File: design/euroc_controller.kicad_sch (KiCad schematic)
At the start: 66 parts, among them J1 xt30, J2 jst_sh 4, J4 jst_sh 4, J5 jst_sh 4, J6 SMA, J8 USB_C_Receptacle_USB2.0, J9 jst_sh 4, Q1 MMBT3904, U1 TPSM5601R5, U13 STM32U575CGTx, U2 USBLC6-2SC6, U3 LSM6DSO32, U4 MS5611-01BA, U5 TCAN332, U6 W25Q128JVS, U7 RFM69W, U8 L86, Y1 48MHz

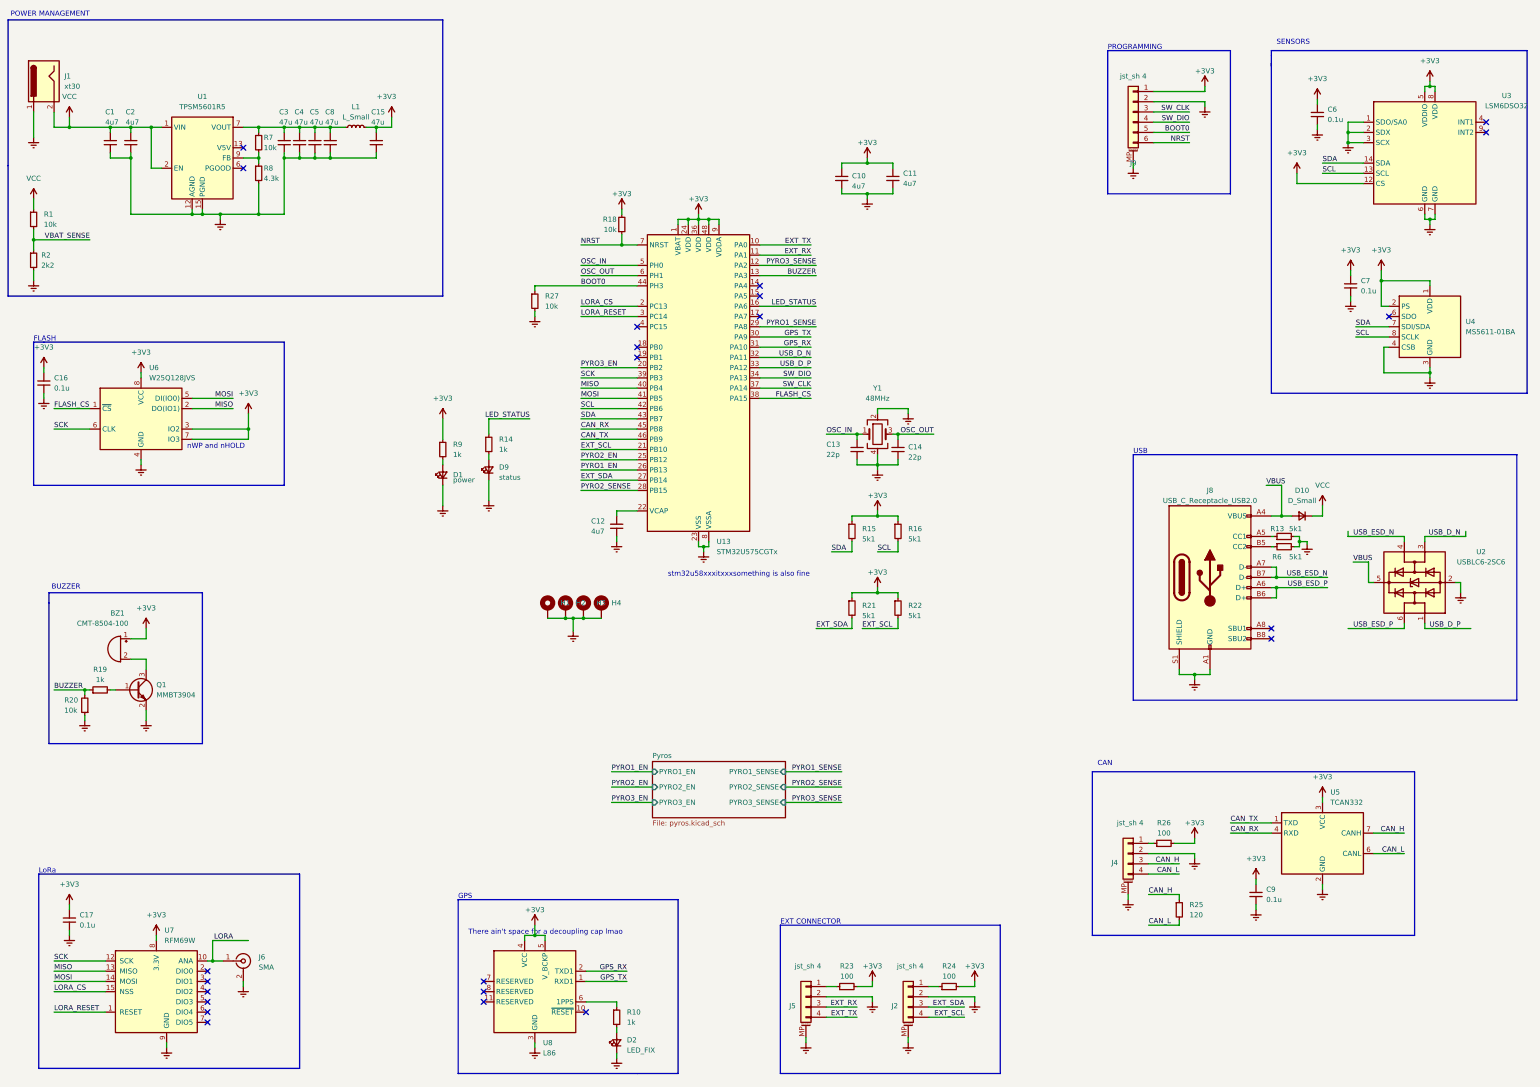
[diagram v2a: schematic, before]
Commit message: PCB 1.1 old regulator
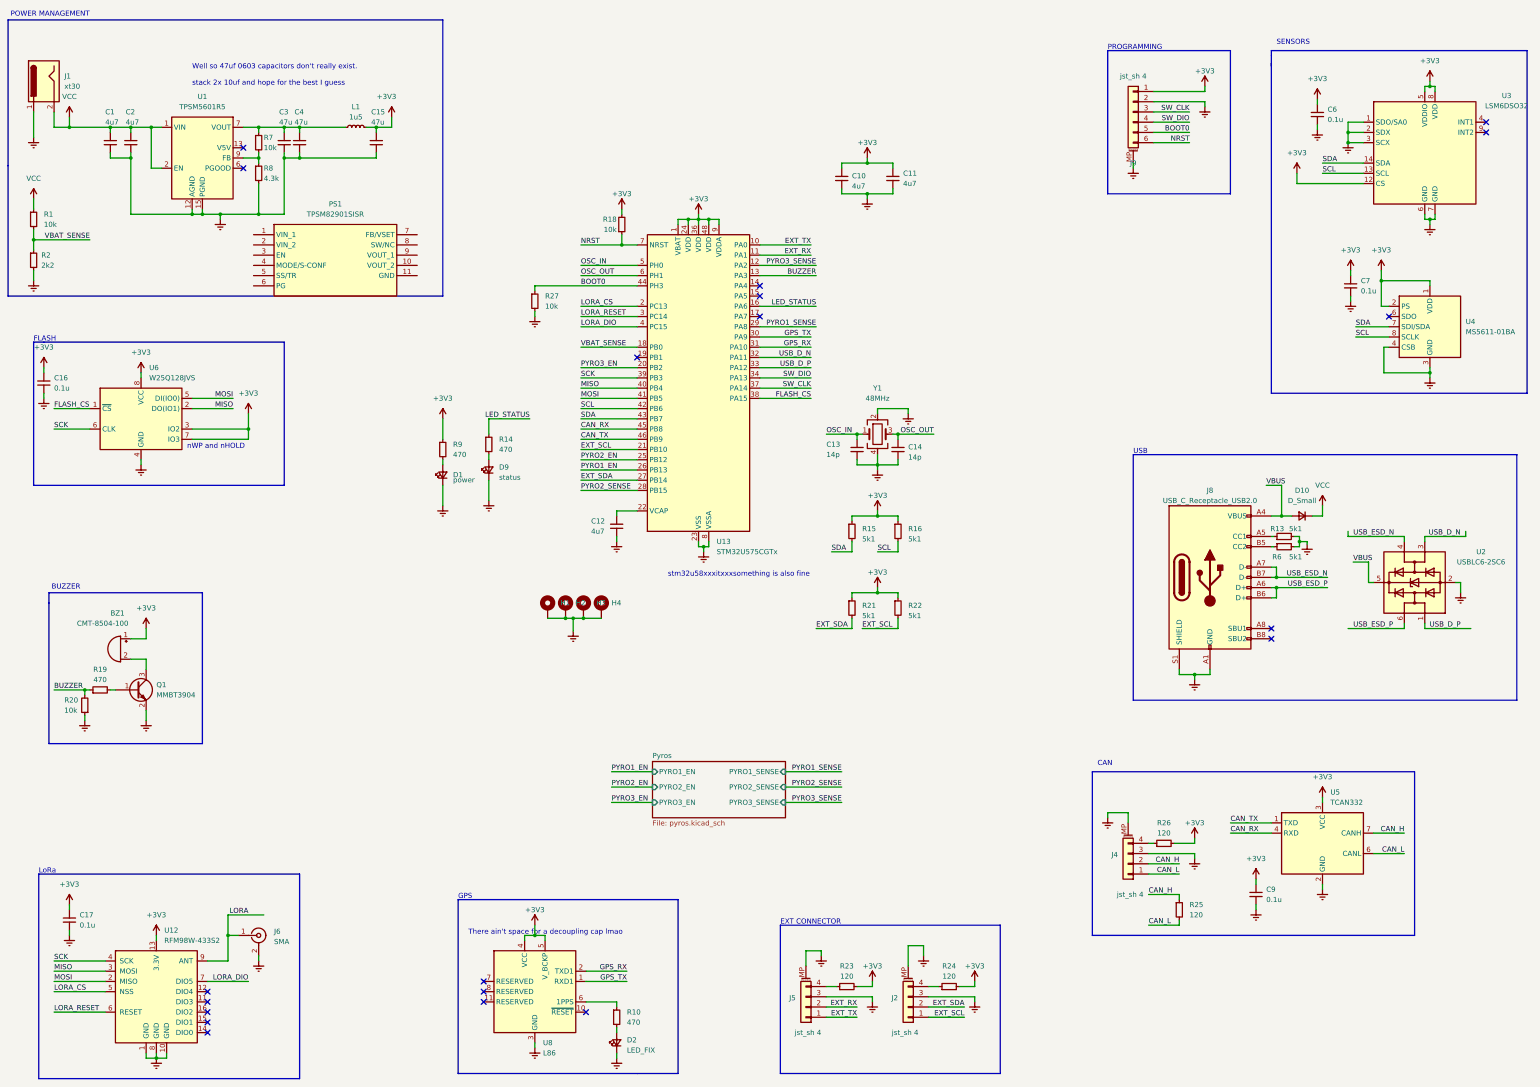
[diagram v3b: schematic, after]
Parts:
- removed C5, C8: 47u, Capacitor_SMD:C_0603_1608Metric, symbol Device:C_Small
- removed U7: RFM69W, RF_Module:HOPERF_RFM69HW, symbol RF_Module:RFM69W
- added PS1: TPSM82901SISR, lib:TPSM82901SISR, symbol TPSM82901SISR:TPSM82901SISR
- added U12: RFM98W-433S2, RF_Module:HOPERF_RFM9XW_SMD, symbol RF_Module:RFM98W-433S2
- C1, C15, C2, C3, C4: footprint Capacitor_SMD:C_0603_1608Metric -> Capacitor_SMD:C_1206_3216Metric
- C13, C14: value 22p -> 14p
- D10: mfn (none) -> BAT760-7
- J2, J4, J5: footprint Connector_JST:JST_SH_BM04B-SRSS-TB_1x04-1MP_P1.00mm_Vertical -> Connector_JST:JST_SH_SM04B-SRSS-TB_1x04-1MP_P1.00mm_Horizontal
- J8: mfn (none) -> USB4105-GF-A
- L1: value L_Small -> 1u5; footprint Inductor_SMD:L_0603_1608Metric -> Inductor_SMD:L_1206_3216Metric; mfn (none) -> MCHK1608T1R5MKN
- R10, R14, R19, R9: value 1k -> 470
- R23, R24, R26: value 100 -> 120
- Y1: mfn (none) -> CX2016SA48000H0FLJG1
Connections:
- net +3V3: now also U12.13 (3.3V)
- net CAN_H: now also J4.2 (Pin_2); no longer J4.3 (Pin_3)
- net CAN_L: now also J4.1 (Pin_1); no longer J4.4 (Pin_4)
- net EXT_RX: now also J5.2 (Pin_2); no longer J5.3 (Pin_3)
- net EXT_SCL: now also J2.1 (Pin_1); no longer J2.4 (Pin_4)
- net EXT_SDA: now also J2.2 (Pin_2); no longer J2.3 (Pin_3)
- net EXT_TX: now also J5.1 (Pin_1); no longer J5.4 (Pin_4)
- net Earth: now also J2.3 (Pin_3), J4.3 (Pin_3), J5.3 (Pin_3), U12.1 (GND), U12.10 (GND), U12.8 (GND); no longer J2.2 (Pin_2), J4.2 (Pin_2), J5.2 (Pin_2)
- net LORA: now also U12.9 (ANT)
- net LORA_CS: now also U12.5 (NSS)
- net LORA_RESET: now also U12.6 (RESET)
- net MISO: now also U12.3 (MOSI)
- net MOSI: now also U12.2 (MISO)
- net SCK: now also U12.4 (SCK)
- net VBAT_SENSE: now also U13.18 (PB0)
- net at R24.1: now also J2.4 (Pin_4); no longer J2.1 (Pin_1)
- net at R26.1: now also J4.4 (Pin_4); no longer J4.1 (Pin_1)
- net at R23.1: now also J5.4 (Pin_4); no longer J5.1 (Pin_1)
- net LORA_DIO: now reaches U13.4 (PC15)
- net LORA_DIO: now also U12.7 (DIO5)
- no-connect marks 23 -> 20
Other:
- note added: "Well so 47uf 0603 capacitors don't really exist. stack 2x 10uf and hope for the best I guess"
- moved on the sheet: J2, J4, J5, J6

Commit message: PCB v1.1
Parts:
- removed C15: 47u, Capacitor_SMD:C_1206_3216Metric, symbol Device:C_Small
- removed U1: TPSM5601R5, Package_DFN_QFN:Texas_B3QFN-14-1EP_5x5.5mm_P0.65mm, symbol Converter_DCDC:TPSM53602RDA
- added C5: 10u, Capacitor_SMD:C_1206_3216Metric, symbol Device:C_Small
- C1: value 4u7 -> N/A; footprint Capacitor_SMD:C_1206_3216Metric -> Capacitor_SMD:C_0603_1608Metric
- C2: value 4u7 -> 10u; mfn (none) -> C3216X7R1E106K160AB
- C3, C4: value 47u -> 22u; footprint Capacitor_SMD:C_1206_3216Metric -> Capacitor_SMD:C_0805_2012Metric; mfn (none) -> C2012X7S1A226M125AC
- D10: footprint Diode_SMD:D_0603_1608Metric -> Diode_SMD:D_SOD-323_HandSoldering
- L1: value 1u5 -> 1u; footprint Inductor_SMD:L_1206_3216Metric -> Inductor_SMD:L_0805_2012Metric; mfn MCHK1608T1R5MKN -> (none)
- R7: value 10k -> N/A
- R8: value 4.3k -> 26k1; footprint Resistor_SMD:R_0603_1608Metric -> Capacitor_SMD:C_0603_1608Metric
- U1: renamed from PS1; footprint lib:TPSM82901SISR -> lib:uSIP11_SIS_TEX
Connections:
- net +3V3: now also C4.1
- net Earth: now also C1.1, C2.1, R7.2, R8.1, U1.11 (GND), C5.2; no longer C1.2, C2.2, R8.2
- net LORA_DIO: now also U12.14 (DIO0); no longer U12.7 (DIO5)
- net VCC: now also C2.2, U1.1 (VIN_1), U1.2 (VIN_2), U1.3 (EN), C5.1; no longer C1.1, C2.1
- net 3v3_raw: now reaches C3.1, L1.1
- net 3v3_raw: now also U1.10 (VOUT_2), U1.9 (VOUT_1); no longer C4.1, R7.1
- net at U1.4 (MODE/S-CONF): now also R8.2
- net at U1.5 (SS/TR): now also C1.2
- net at U1.7 (FB/VSET): now also R7.1
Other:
- note added: "Add an unnecessary resistor because why not"
- note added: "C2 and C3 have recommened part numbers"
- note added: "FB/VSET open to select 3.3v"
- note added: "Mode R set to 26k1 for 2.5MHz Auto pwm Auto efficiency set voltage"
- note added: "Only C2 andC3 are in the datasheet's typical application"
- note added: "SS/TR controls rise time. Can be left open"
- note removed: "Well so 47uf 0603 capacitors don't really exist. stack 2x 10uf and hope for the best I guess"
- moved on the sheet: U1

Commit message: v1.2
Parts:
- removed J2, J4, J5: jst_sh 4, Connector_JST:JST_SH_SM04B-SRSS-TB_1x04-1MP_P1.00mm_Horizontal, symbol Connector_Generic_MountingPin:Conn_01x04_MountingPin
- removed L1: 1u, Inductor_SMD:L_0805_2012Metric, symbol Device:L_Small
- removed R21, R22: 5k1, Resistor_SMD:R_0603_1608Metric, symbol Device:R_Small
- removed R23, R24, R26: 120, Resistor_SMD:R_0805_2012Metric, symbol Device:R_Small
- removed R7: N/A, Resistor_SMD:R_0603_1608Metric, symbol Device:R_Small
- removed R8: 26k1, Capacitor_SMD:C_0603_1608Metric, symbol Device:R_Small
- removed U1: TPSM82901SISR, lib:uSIP11_SIS_TEX, symbol TPSM82901SISR:TPSM82901SISR
- added C15, C8: 1u, Capacitor_SMD:C_0603_1608Metric, symbol Device:C_Small
- added C18, C19: 10u, Capacitor_SMD:C_0603_1608Metric, symbol Device:C_Small
- added C20: 220n, Capacitor_SMD:C_0603_1608Metric, symbol Device:C_Small
- added C21: 100n, Capacitor_SMD:C_0603_1608Metric, symbol Device:C_Small
- added FB2, FB4: BLM18KG102SN1D, Inductor_SMD:L_0805_2012Metric_Pad1.15x1.40mm_HandSolder, symbol Device:FerriteBead_Small
- added IC1: LMR50410Y3, Package_TO_SOT_SMD:SOT-23-6_Handsoldering, symbol LMR50410YQDBVRQ1:LMR50410YQDBVRQ1
- added J2: jst gh 6, Connector_JST:JST_GH_SM06B-GHS-TB_1x06-1MP_P1.25mm_Horizontal, symbol Connector_Generic_MountingPin:Conn_01x06_MountingPin
- added J3: jst gh 4, Connector_JST:JST_GH_SM04B-GHS-TB_1x04-1MP_P1.25mm_Horizontal, symbol Connector_Generic_MountingPin:Conn_01x04_MountingPin
- added JP1, JP2: SolderJumper_2_Open, Jumper:SolderJumper-2_P1.3mm_Open_TrianglePad1.0x1.5mm, symbol Jumper:SolderJumper_2_Open
- added L2: 4.7u, Inductor_SMD_Wurth:L_Wurth_WE-LQSH-3012, symbol Device:L_Small
- added SW1: SW_SPST, Button_Switch_SMD:SW_SPST_B3U-1000P, symbol Switch:SW_SPST
- added U7: LIS2MDL, Package_LGA:LGA-12_2x2mm_P0.5mm, symbol Sensor_Magnetic:LIS2MDL
- C1: value N/A -> 1u
- C2: value 10u -> 1u; footprint Capacitor_SMD:C_1206_3216Metric -> Capacitor_SMD:C_0603_1608Metric; mfn C3216X7R1E106K160AB -> (none)
- C3: value 22u -> 1u; footprint Capacitor_SMD:C_0805_2012Metric -> Capacitor_SMD:C_0603_1608Metric; mfn C2012X7S1A226M125AC -> (none)
- C4: value 22u -> 100n; footprint Capacitor_SMD:C_0805_2012Metric -> Capacitor_SMD:C_0603_1608Metric; mfn C2012X7S1A226M125AC -> (none)
- C5: value 10u -> 100n; footprint Capacitor_SMD:C_1206_3216Metric -> Capacitor_SMD:C_0603_1608Metric; mfn C3216X7R1E106K160AB -> (none)
- J9: value jst_sh 4 -> jst_sh 6
- U8: value L86 -> LC86
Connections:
- net 3v3_raw is gone; now on net Earth: C3.1
- net +3V3: now also C15.2, C21.1, FB4.1, J2.1 (Pin_1), SW1.2 (B), U7.10 (Vdd_IO), U7.3 (~{CS}), U7.9 (Vdd); no longer C4.1
- net BOOT0: now also SW1.1 (A)
- net CAN_H: now also J3.2 (Pin_2), JP2.2 (B); no longer R25.1
- net CAN_L: now also J3.3 (Pin_3)
- net EXT_RX: now also J2.2 (Pin_2)
- net EXT_TX: now also J2.3 (Pin_3)
- net Earth: now also C4.1, C15.1, C18.2, C19.2, C20.2, C21.2, C8.1, IC1.2 (GND), J2.6 (Pin_6), J2.MP (MountPin), J3.4 (Pin_4), J3.MP (MountPin), U7.6 (GND), U7.8 (GND); no longer C3.2, C4.2, C5.2
- net MISO: now also U12.2 (MISO); no longer U12.3 (MOSI)
- net MOSI: now also U12.3 (MOSI); no longer U12.2 (MISO)
- net SCL: now also U7.1 (SCL/SPC)
- net SDA: now also U7.4 (SDA/SDI/SDO)
- net VCC: now also C1.2, FB2.2, JP1.1 (A); no longer C2.2, C5.1
- net EXT_IO1: now reaches U13.14 (PA4)
- net EXT_IO1: now also J2.5 (Pin_5)
- net EXT_IO0: now reaches U13.15 (PA5)
- net EXT_IO0: now also J2.4 (Pin_4)
- new net: J3.1 (Pin_1), JP1.2 (B)
- new net: C20.1, U7.5 (C1)
- new net: JP2.1 (A), R25.1
- new net CB: C5.1, IC1.1 (CB)
- new net OUT_RAW: C18.1, C19.1, C8.2, FB4.2, IC1.3 (FB), L2.2
- new net SW: C5.2, IC1.6 (SW), L2.1
- new net VCC_FILT: C2.2, C3.2, C4.2, FB2.1, IC1.4 (EN), IC1.5 (VIN)
- no-connect marks 20 -> 17
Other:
- note removed: "Add an unnecessary resistor because why not"
- note removed: "C2 and C3 have recommened part numbers"
- note removed: "FB/VSET open to select 3.3v"
- note removed: "Mode R set to 26k1 for 2.5MHz Auto pwm Auto efficiency set voltage"
- note removed: "Only C2 andC3 are in the datasheet's typical application"
- note removed: "SS/TR controls rise time. Can be left open"
- moved on the sheet: J1
